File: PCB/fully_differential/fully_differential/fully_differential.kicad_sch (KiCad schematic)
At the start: 38 parts, among them U1 LM741, U2 LM741, U3 LM741, U4 LM741, U5 LM324, U6 AD8138, U7 LM324

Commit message: new pcb
falta validar para impressao
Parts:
- removed R1: R, Resistor_THT:R_Axial_DIN0207_L6.3mm_D2.5mm_P10.16mm_Horizontal, symbol Device:R
- removed unit 1 of U5
- removed unit 2 of U5
- removed unit 3 of U5
- removed unit 5 of U7
- added C1, C2, C3, C4: C, Capacitor_THT:CP_Radial_D5.0mm_P2.00mm, symbol Device:C
- added J1, J2, J3, J4, J5: Conn_01x03, Connector_PinHeader_2.54mm:PinHeader_1x03_P2.54mm_Vertical, symbol Connector_Generic:Conn_01x03
- added J10: PIN_A0, Connector_PinHeader_2.54mm:PinHeader_1x01_P2.54mm_Vertical, symbol Connector_Generic:Conn_01x01
- added J11: PIN_09, Connector_PinHeader_2.54mm:PinHeader_1x01_P2.54mm_Vertical, symbol Connector_Generic:Conn_01x01
- added J6, J7, J8: Conn_01x01, Connector_PinHeader_2.54mm:PinHeader_1x01_P2.54mm_Vertical, symbol Connector_Generic:Conn_01x01
- added J9: Conn_01x03, Connector_Stocko:Stocko_MKS_1653-6-0-303_1x3_P2.50mm_Vertical, symbol Connector_Generic:Conn_01x03
- added U4: L7805, l7805:TO255P1020X450X2000-3, symbol Regulator_Linear:L7805
- added U7: L7905, TO255P1020X450X2000-3, symbol Regulator_Linear:L7905
- added U9: LM324, lm324:DIP825W47P254L1917H533Q14, symbol Amplifier_Operational:LM324
- C5: renamed from C1; footprint Capacitor_THT:C_Rect_L24.0mm_W7.0mm_P22.50mm_MKT -> Capacitor_THT:C_Rect_L19.0mm_W6.0mm_P15.00mm_MKS4
- RV1, RV2, RV3, RV4: footprint Potentiometer_THT:Potentiometer_Runtron_RM-065_Vertical -> Potentiometer_THT:Potentiometer_Bourns_3296W_Vertical
- renumbered R3 to R1, R24 to R10, R23 to R11, R6 to R12, R2 to R13, R9 to R14, R26 to R15, R19 to R16, R25 to R17, R21 to R18, R14 to R19, R10 to R2, R4 to R20, R11 to R21, R17 to R22, R12 to R23, R18 to R24, R13 to R25, R5 to R3, R15 to R4, R8 to R5, R20 to R6, R22 to R7, R7 to R8, R16 to R9, U4 to U1, U1 to U2, U6 to U3, U7 to U5, U2 to U6, U3 to U8
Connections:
- net +5V: now also C2.1, U4.3 (OUT)
- net +9V: now also C1.1, J9.3 (Pin_3), U4.1 (IN), U9.4 (V+)
- net -5V: now also C4.2, U7.3 (VO)
- net -9V: now also C3.2, J2.1 (Pin_1), J9.1 (Pin_1), U7.2 (VI), U9.11 (V-); no longer RV1.2, RV2.2, RV3.2, RV4.2
- net GND: now also C1.2, C2.2, C3.1, C4.1, J9.2 (Pin_2), U4.2 (GND), U7.1 (GND), U9.10 (+)
- net op1_1: now also J1.1 (Pin_1); no longer RV1.3
- net op2_1: now also J3.1 (Pin_1); no longer RV2.3
- net op3_1: now also J4.1 (Pin_1); no longer RV3.3
- net op4_1: now also J5.1 (Pin_1); no longer RV4.3
- net t+: now also U9.7
- net t-: now also U9.8
- net at R4.2: now also J6.1 (Pin_1); no longer U2.3 (+)
- net at R9.1, U5.5 (+), U6.3 (+): now also J8.1 (Pin_1)
- net at R22.2, R24.1: now also U9.9 (-)
- net at R23.2, R25.1: now also U9.6 (-)
- net at R19.1, R21.2: now also U9.5 (+)
- net at R21.1: now also U9.1, U9.2 (-)
- net at C5.1, R20.2: now also U9.3 (+)
- net A0: no longer names the net of R15.1, U5.14
- net A0: now also J10.1 (Pin_1)
- net v+: no longer names the net of R20.1
- net v+: now also J11.1 (Pin_1)
- new net: J4.2 (Pin_2), RV3.3
- new net: J1.2 (Pin_2), RV1.3
- new net: J5.2 (Pin_2), RV4.3
- new net: J2.2 (Pin_2), RV1.2, RV2.2, RV3.2, RV4.2
- new net: J7.1 (Pin_1), U2.3 (+)
- new net: J3.2 (Pin_2), RV2.3
- no-connect marks 2 -> 10
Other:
- company: (none) -> Felipe Avila Silva
- title: (none) -> Fully Differential Potentiostat
- moved on the sheet: C5, R20, RV1, RV2, RV3, RV4, U5E

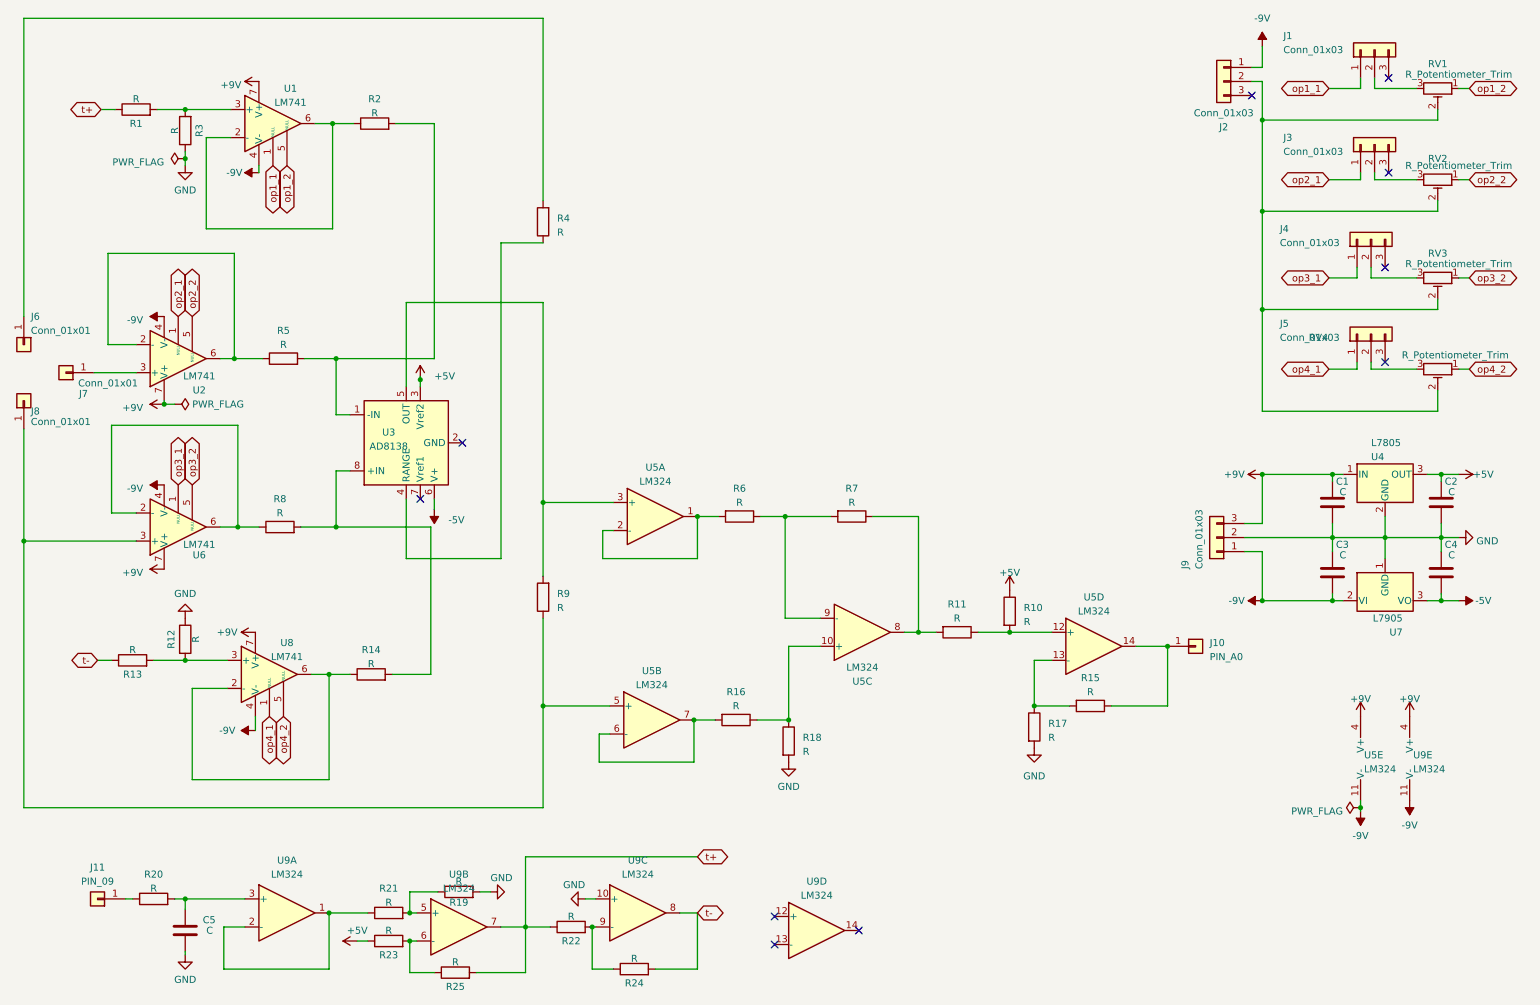
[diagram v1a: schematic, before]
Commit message: pcb finalizado
falta retirar divisor de tensao e mudar a leitura da tensao no resistor superior
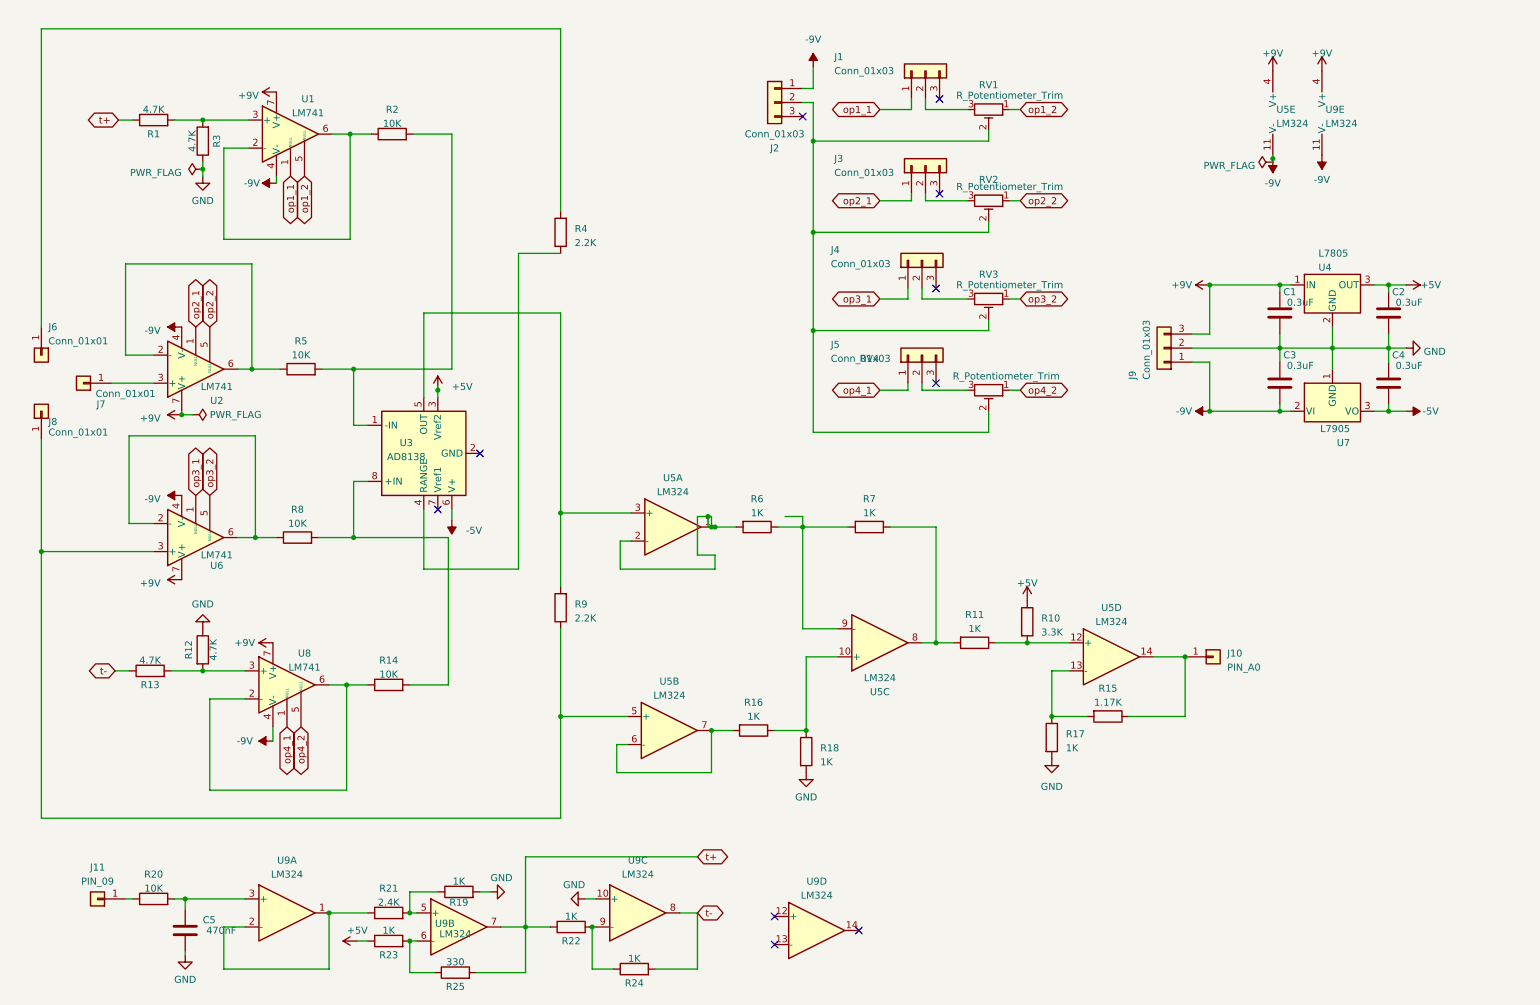
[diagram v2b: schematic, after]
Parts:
- C1, C2, C3, C4: value C -> 0.3uF
- C5: value C -> 470nF
- R1, R12, R13, R3: value R -> 4.7K
- R10: value R -> 3.3K
- R11, R16, R17, R18, R19, R22, R23, R24, R6, R7: value R -> 1K
- R14, R2, R20, R5, R8: value R -> 10K
- R15: value R -> 1.17K
- R21: value R -> 2.4K
- R25: value R -> 330
- R4, R9: value R -> 2.2K
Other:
- moved on the sheet: C1, C2, C3, C4, J1, J10, J2, J3, J4, J5, J6, J7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

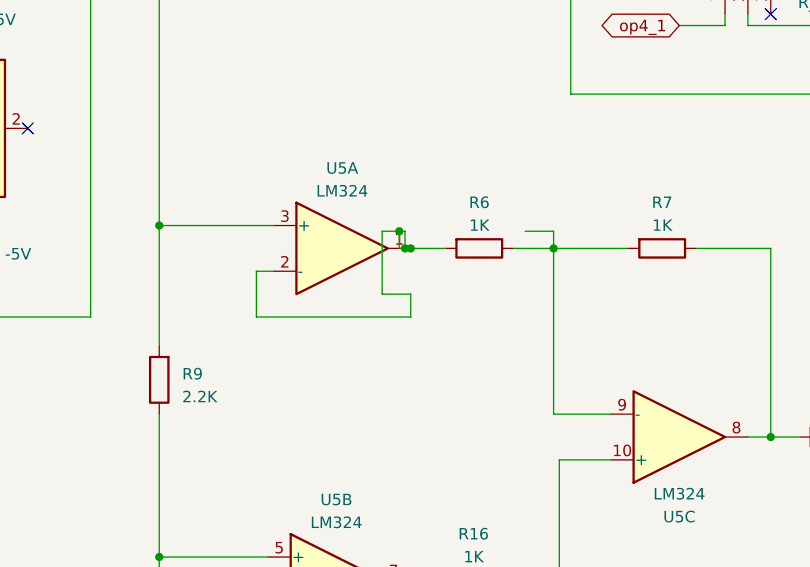
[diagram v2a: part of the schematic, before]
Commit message: fix proteus 1.5v and 3v
stock v2 proteus and kicad ok
fully v4 proteus and kicad ok
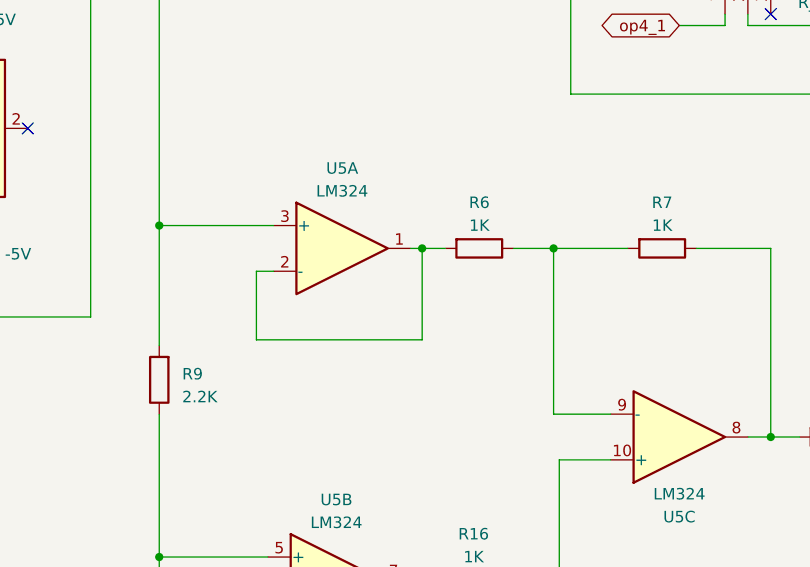
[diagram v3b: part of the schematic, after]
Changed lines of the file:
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@@
   (junction (at 156.845 36.195) (diameter 0) (color 0 0 0 0)
   )
-  (junction (at 139.065 106.045) (diameter 0) (color 0 0 0 0)
-  )
   (junction (at 241.3 73.66) (diameter 0) (color 0 0 0 0)
   )
   (junction (at 42.545 85.725) (diameter 0) (color 0 0 0 0)
   )
-  (junction (at 138.43 106.045) (diameter 0) (color 0 0 0 0)
-  )
   (junction (at 83.82 180.975) (diameter 0) (color 0 0 0 0)
   )
@@
   (junction (at 179.07 127) (diameter 0) (color 0 0 0 0)
   )
+  (junction (at 140.335 106.045) (diameter 0) (color 0 0 0 0)
+  )
   (junction (at 55.245 77.47) (diameter 0) (color 0 0 0 0)
   )
@@
   )
   (junction (at 83.82 175.895) (diameter 0) (color 0 0 0 0)
-  )
-  (junction (at 137.795 104.14) (diameter 0) (color 0 0 0 0)
   )
   (junction (at 260.985 73.66) (diameter 0) (color 0 0 0 0)
@@
     (stroke (width 0) (type default))
   )
-  (wire (pts (xy 121.92 113.665) (xy 139.065 113.665))
-    (stroke (width 0) (type default))
-  )
-  (wire (pts (xy 139.065 106.045) (xy 142.875 106.045))
+  (wire (pts (xy 121.92 116.205) (xy 140.335 116.205))
     (stroke (width 0) (type default))
   )
@@
     (stroke (width 0) (type default))
   )
+  (wire (pts (xy 140.335 106.045) (xy 142.875 106.045))
+    (stroke (width 0) (type default))
+  )
   (wire (pts (xy 200.025 132.08) (xy 200.025 140.335))
     (stroke (width 0) (type default))
@@
     (stroke (width 0) (type default))
   )
-  (wire (pts (xy 138.43 106.045) (xy 138.43 104.14))
-    (stroke (width 0) (type default))
-  )
   (wire (pts (xy 123.19 145.415) (xy 121.285 145.415))
     (stroke (width 0) (type default))
@@
     (stroke (width 0) (type default))
   )
-  (wire (pts (xy 139.065 106.045) (xy 138.43 106.045))
-    (stroke (width 0) (type default))
-  )
-  (wire (pts (xy 135.89 111.125) (xy 135.89 104.14))
-    (stroke (width 0) (type default))
-  )
   (wire (pts (xy 50.165 178.435) (xy 50.165 186.055))
     (stroke (width 0) (type default))
@@
     (stroke (width 0) (type default))
   )
-  (wire (pts (xy 137.795 106.045) (xy 137.795 104.14))
-    (stroke (width 0) (type default))
-  )
   (wire (pts (xy 73.66 77.47) (xy 91.44 77.47))
     (stroke (width 0) (type default))
@@
     (stroke (width 0) (type default))
   )
-  (wire (pts (xy 139.065 113.665) (xy 139.065 111.125))
+  (wire (pts (xy 140.335 106.045) (xy 140.335 116.205))
     (stroke (width 0) (type default))
   )
@@
     (stroke (width 0) (type default))
   )
-  (wire (pts (xy 138.43 104.14) (xy 137.795 104.14))
-    (stroke (width 0) (type default))
-  )
   (wire (pts (xy 90.805 134.62) (xy 90.805 107.95))
     (stroke (width 0) (type default))
@@
     (stroke (width 0) (type default))
   )
-  (wire (pts (xy 154.94 104.14) (xy 151.765 104.14))
-    (stroke (width 0) (type default))
-  )
   (wire (pts (xy 121.285 145.415) (xy 121.285 150.495))
     (stroke (width 0) (type default))
@@
     (stroke (width 0) (type default))
   )
-  (wire (pts (xy 138.43 106.045) (xy 137.795 106.045))
-    (stroke (width 0) (type default))
-  )
   (wire (pts (xy 135.89 165.735) (xy 104.775 165.735))
     (stroke (width 0) (type default))
@@
     (stroke (width 0) (type default))
   )
-  (wire (pts (xy 121.92 108.585) (xy 121.92 113.665))
+  (wire (pts (xy 121.92 108.585) (xy 121.92 116.205))
     (stroke (width 0) (type default))
   )
@@
     (stroke (width 0) (type default))
   )
-  (wire (pts (xy 139.065 111.125) (xy 135.89 111.125))
-    (stroke (width 0) (type default))
-  )
   (wire (pts (xy 194.31 81.28) (xy 192.405 81.28))
     (stroke (width 0) (type default))
@@
     (stroke (width 0) (type default))
   )
-  (wire (pts (xy 154.94 106.045) (xy 154.94 104.14))
-    (stroke (width 0) (type default))
-  )
   (wire (pts (xy 188.595 70.485) (xy 156.845 70.485))
     (stroke (width 0) (type default))
@@
     (stroke (width 0) (type default))
   )
-  (wire (pts (xy 137.795 104.14) (xy 135.89 104.14))
-    (stroke (width 0) (type default))
-  )
   (wire (pts (xy 188.595 68.58) (xy 188.595 70.485))
     (stroke (width 0) (type default))
@@
     (stroke (width 0) (type default))
   )
+  (wire (pts (xy 139.065 106.045) (xy 140.335 106.045))
+    (stroke (width 0) (type default))
+  )
